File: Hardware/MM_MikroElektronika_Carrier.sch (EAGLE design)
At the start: 51 parts, among them J15 MICROMOD-2222-C, J2 QWIIC_RIGHT_ANGLE, J5 Vertical Qwiic Connector, U1 MCP73831, U5 AP7361C-33FGEUDFN-8

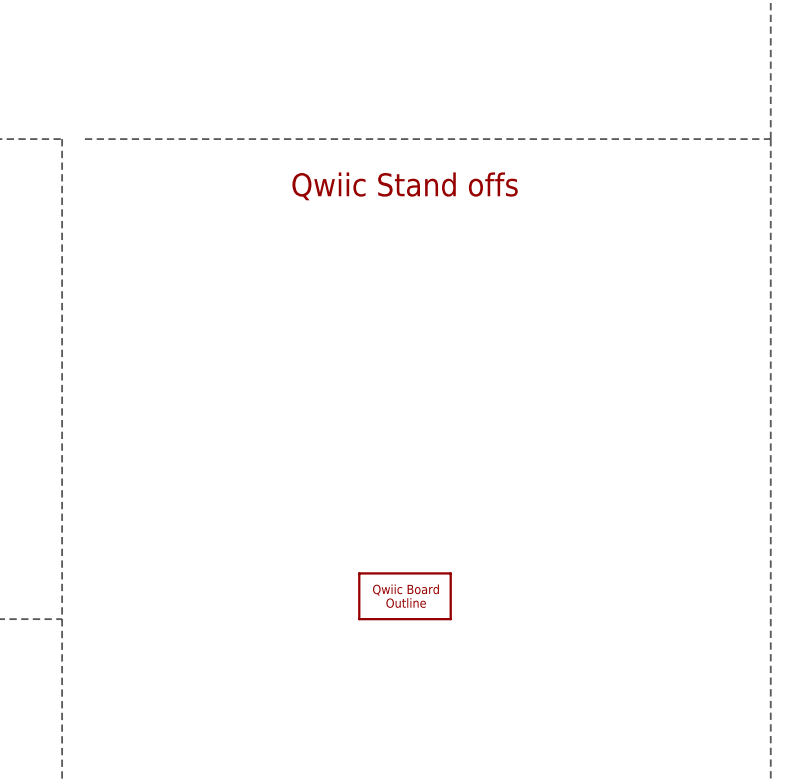
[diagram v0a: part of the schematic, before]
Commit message: Renamed eagle files
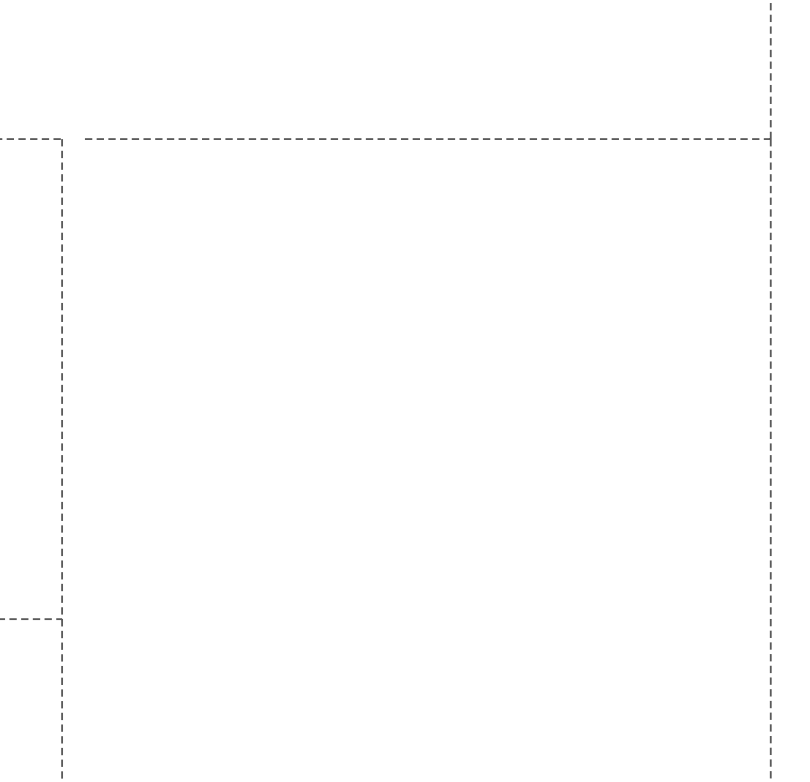
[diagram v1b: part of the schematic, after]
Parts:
- removed U$5: QWIIC_BOARD_OUTLINESTANDOFF, SparkFun-Boards:QWIIC_BOARD_OUTLINESTANDOFF
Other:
- note removed: "Qwiic Stand offs"
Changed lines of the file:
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@@
 <?xml version="1.0" encoding="utf-8"?>
 <!DOCTYPE eagle SYSTEM "eagle.dtd">
-<eagle version="9.5.2">
+<eagle version="9.4.2">
 <drawing>
 <settings>
-<setting alwaysvectorfont="no"/>
+<setting alwaysvectorfont="yes"/>
 <setting verticaltext="up"/>
 </settings>
@@
 <part name="SUPPLY14" library="SparkFun-PowerSymbols" deviceset="3.3V" device=""/>
 <part name="GND26" library="SparkFun-PowerSymbols" deviceset="GND" device=""/>
-<part name="U$5" library="SparkFun-Boards" deviceset="QWIIC_BOARD_OUTLINE" device="STANDOFF"/>
 <part name="SUPPLY15" library="SparkFun-PowerSymbols" deviceset="V_USB_2" device=""/>
 <part name="SUPPLY16" library="SparkFun-PowerSymbols" deviceset="V_USB_2" device=""/>
@@
 <text x="210.82" y="104.14" size="2.54" layer="94" font="vector" align="center">Buttons</text>
 <text x="259.08" y="180.34" size="2.54" layer="94" font="vector" align="center">Battery Charger</text>
-<text x="289.56" y="106.68" size="2.54" layer="94" font="vector" align="center">Qwiic Stand offs</text>
 <wire x1="254" y1="111.76" x2="330.2" y2="111.76" width="0.2032" layer="97" style="longdash"/>
 <wire x1="330.2" y1="111.76" x2="330.2" y2="38.1" width="0.2032" layer="97" style="longdash"/>
@@
 <attribute name="VALUE" x="210.82" y="9.906" size="1.778" layer="96" align="top-center"/>
 </instance>
-<instance part="U$5" gate="G$1" x="289.56" y="60.96" smashed="yes"/>
 <instance part="SUPPLY15" gate="G$1" x="396.24" y="147.32" smashed="yes">
 <attribute name="VALUE" x="396.24" y="150.114" size="1.778" layer="96" align="bottom-center"/>
